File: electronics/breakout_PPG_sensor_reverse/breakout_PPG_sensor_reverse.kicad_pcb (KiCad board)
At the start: 2 copper layers, 19.1 x 11.5 mm, 4 parts, among them J1 Conn_01x04, J2 Conn_01x04, U1 PPG_sensor

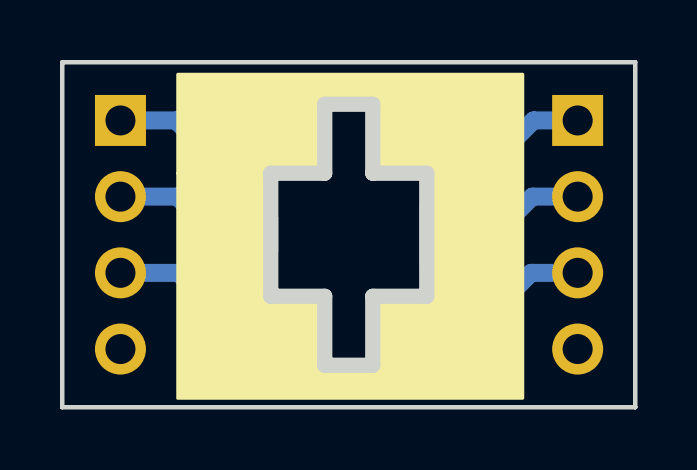
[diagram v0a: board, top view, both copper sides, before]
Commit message: changed cutouts for the PPG sensor, oshpark seems to compute cutouts differently then eagle somehow?
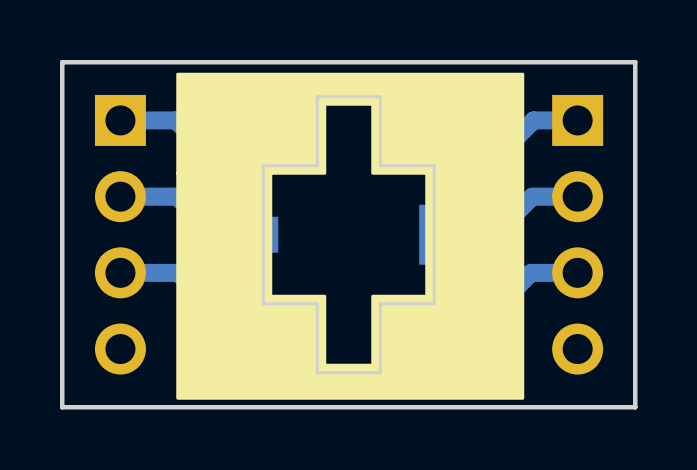
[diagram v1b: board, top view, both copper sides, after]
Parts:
- N2: value 20200709 -> 20200809
- U1: footprint SquantorOpto:PPG_sensor_reverse -> SquantorOpto:PPG_sensor_reverse_PD_parallel
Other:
- outline, holes or cut-outs redrawn
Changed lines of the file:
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@@
-(kicad_pcb (version 20171130) (host pcbnew 5.1.6-c6e7f7d~86~ubuntu19.10.1)
+(kicad_pcb (version 20171130) (host pcbnew 5.1.6-c6e7f7d~87~ubuntu19.10.1)
   (general
     (thickness 1.6)
@@
   )
   (setup
-    (last_trace_width 0.6)
+    (last_trace_width 0.1524)
     (user_trace_width 0.1524)
     (user_trace_width 0.2)
@@
     (uvia_min_size 0.381)
     (uvia_min_drill 0.254)
-    (edge_width 0.508)
+    (edge_width 0.1)
     (segment_width 0.2)
     (pcb_text_width 0.3)
@@
     (add_net /VSS)
   )
-  (module SquantorOpto:PPG_sensor_reverse (layer F.Cu)
+  (module SquantorOpto:PPG_sensor_reverse_PD_parallel (layer F.Cu)
     (at 162.55 101.6)
-    (descr "combination of SFH2440 reverse mount with 1206 reverse mount LEDS")
+    (descr "combination of SFH2440 reverse mount parallel with 3216 reverse mount LEDS")
     (tags "PPG sensor")
-    (fp_text reference U1 (at 0 -5) (layer B.SilkS)
-      (effects (font (size 1 1) (thickness 0.15)) (justify mirror))
-    )
-    (fp_text value PPG_sensor (at 0 4.6) (layer B.Fab)
+    (fp_text reference U1 (at 0 -5.2) (layer B.SilkS)
+      (effects (font (size 1 1) (thickness 0.15)) (justify mirror))
+    )
+    (fp_text value PPG_sensor (at 0 5) (layer B.Fab)
       (effects (font (size 1 1) (thickness 0.15)) (justify mirror))
     )
@@
       (effects (font (size 1 1) (thickness 0.15)) (justify mirror))
     )
+    (fp_line (start 1.8 1.8) (end -1.8 1.8) (layer B.CrtYd) (width 0.05))
+    (fp_line (start 1.8 -9.4) (end 1.8 1.8) (layer B.CrtYd) (width 0.05))
+    (fp_line (start -1.8 -9.4) (end 1.8 -9.4) (layer B.CrtYd) (width 0.05))
+    (fp_line (start -1.8 1.8) (end -1.8 -9.4) (layer B.CrtYd) (width 0.05))
+    (fp_line (start -1.33 1.33) (end 0 1.33) (layer B.SilkS) (width 0.12))
+    (fp_line (start -1.33 0) (end -1.33 1.33) (layer B.SilkS) (width 0.12))
+    (fp_line (start -1.33 -1.27) (end 1.33 -1.27) (layer B.SilkS) (width 0.12))
+    (fp_line (start 1.33 -1.27) (end 1.33 -8.95) (layer B.SilkS) (width 0.12))
+    (fp_line (start -1.33 -1.27) (end -1.33 -8.95) (layer B.SilkS) (width 0.12))
+    (fp_line (start -1.33 -8.95) (end 1.33 -8.95) (layer B.SilkS) (width 0.12))
+    (fp_line (start -1.27 0.635) (end -0.635 1.27) (layer B.Fab) (width 0.1))
+    (fp_line (start -1.27 -8.89) (end -1.27 0.635) (layer B.Fab) (width 0.1))
+    (fp_line (start 1.27 -8.89) (end -1.27 -8.89) (layer B.Fab) (width 0.1))
+    (fp_line (start 1.27 1.27) (end 1.27 -8.89) (layer B.Fab) (width 0.1))
     (fp_line (start -0.635 1.27) (end 1.27 1.27) (layer B.Fab) (width 0.1))
-    (fp_line (start 1.27 1.27) (end 1.27 -8.89) (layer B.Fab) (width 0.1))
-    (fp_line (start 1.27 -8.89) (end -1.27 -8.89) (layer B.Fab) (width 0.1))
-    (fp_line (start -1.27 -8.89) (end -1.27 0.635) (layer B.Fab) (width 0.1))
-    (fp_line (start -1.27 0.635) (end -0.635 1.27) (layer B.Fab) (width 0.1))
-    (fp_line (start -1.33 -8.95) (end 1.33 -8.95) (layer B.SilkS) (width 0.12))
-    (fp_line (start -1.33 -1.27) (end -1.33 -8.95) (layer B.SilkS) (width 0.12))
-    (fp_line (start 1.33 -1.27) (end 1.33 -8.95) (layer B.SilkS) (width 0.12))
-    (fp_line (start -1.33 -1.27) (end 1.33 -1.27) (layer B.SilkS) (width 0.12))
-    (fp_line (start -1.33 0) (end -1.33 1.33) (layer B.SilkS) (width 0.12))
-    (fp_line (start -1.33 1.33) (end 0 1.33) (layer B.SilkS) (width 0.12))
-    (fp_line (start -1.8 1.8) (end -1.8 -9.4) (layer B.CrtYd) (width 0.05))
-    (fp_line (start -1.8 -9.4) (end 1.8 -9.4) (layer B.CrtYd) (width 0.05))
-    (fp_line (start 1.8 -9.4) (end 1.8 1.8) (layer B.CrtYd) (width 0.05))
-    (fp_line (start 1.8 1.8) (end -1.8 1.8) (layer B.CrtYd) (width 0.05))
     (fp_text user %R (at 0 -3.81 270) (layer B.Fab)
       (effects (font (size 1 1) (thickness 0.15)) (justify mirror))
@@
       (effects (font (size 1 1) (thickness 0.15)) (justify mirror))
     )
+    (fp_line (start 1.8 1.8) (end -1.8 1.8) (layer B.CrtYd) (width 0.05))
+    (fp_line (start 1.8 -9.4) (end 1.8 1.8) (layer B.CrtYd) (width 0.05))
+    (fp_line (start -1.8 -9.4) (end 1.8 -9.4) (layer B.CrtYd) (width 0.05))
+    (fp_line (start -1.8 1.8) (end -1.8 -9.4) (layer B.CrtYd) (width 0.05))
+    (fp_line (start -1.33 1.33) (end 0 1.33) (layer B.SilkS) (width 0.12))
+    (fp_line (start -1.33 0) (end -1.33 1.33) (layer B.SilkS) (width 0.12))
+    (fp_line (start -1.33 -1.27) (end 1.33 -1.27) (layer B.SilkS) (width 0.12))
+    (fp_line (start 1.33 -1.27) (end 1.33 -8.95) (layer B.SilkS) (width 0.12))
+    (fp_line (start -1.33 -1.27) (end -1.33 -8.95) (layer B.SilkS) (width 0.12))
+    (fp_line (start -1.33 -8.95) (end 1.33 -8.95) (layer B.SilkS) (width 0.12))
+    (fp_line (start -1.27 0.635) (end -0.635 1.27) (layer B.Fab) (width 0.1))
+    (fp_line (start -1.27 -8.89) (end -1.27 0.635) (layer B.Fab) (width 0.1))
+    (fp_line (start 1.27 -8.89) (end -1.27 -8.89) (layer B.Fab) (width 0.1))
+    (fp_line (start 1.27 1.27) (end 1.27 -8.89) (layer B.Fab) (width 0.1))
     (fp_line (start -0.635 1.27) (end 1.27 1.27) (layer B.Fab) (width 0.1))
-    (fp_line (start 1.27 1.27) (end 1.27 -8.89) (layer B.Fab) (width 0.1))
-    (fp_line (start 1.27 -8.89) (end -1.27 -8.89) (layer B.Fab) (width 0.1))
-    (fp_line (start -1.27 -8.89) (end -1.27 0.635) (layer B.Fab) (width 0.1))
-    (fp_line (start -1.27 0.635) (end -0.635 1.27) (layer B.Fab) (width 0.1))
-    (fp_line (start -1.33 -8.95) (end 1.33 -8.95) (layer B.SilkS) (width 0.12))
-    (fp_line (start -1.33 -1.27) (end -1.33 -8.95) (layer B.SilkS) (width 0.12))
-    (fp_line (start 1.33 -1.27) (end 1.33 -8.95) (layer B.SilkS) (width 0.12))
-    (fp_line (start -1.33 -1.27) (end 1.33 -1.27) (layer B.SilkS) (width 0.12))
-    (fp_line (start -1.33 0) (end -1.33 1.33) (layer B.SilkS) (width 0.12))
-    (fp_line (start -1.33 1.33) (end 0 1.33) (layer B.SilkS) (width 0.12))
-    (fp_line (start -1.8 1.8) (end -1.8 -9.4) (layer B.CrtYd) (width 0.05))
-    (fp_line (start -1.8 -9.4) (end 1.8 -9.4) (layer B.CrtYd) (width 0.05))
-    (fp_line (start 1.8 -9.4) (end 1.8 1.8) (layer B.CrtYd) (width 0.05))
-    (fp_line (start 1.8 1.8) (end -1.8 1.8) (layer B.CrtYd) (width 0.05))
     (fp_text user %R (at 0 -3.81 270) (layer B.Fab)
       (effects (font (size 1 1) (thickness 0.15)) (justify mirror))
@@
       (effects (font (size 1 1) (thickness 0.15)) (justify mirror))
     )
-    (fp_text value 20200709 (at -0.4 0.1 90) (layer B.SilkS)
+    (fp_text value 20200809 (at -0.4 0.1 90) (layer B.SilkS)
       (effects (font (size 1 1) (thickness 0.15)) (justify mirror))
     )
@@
     )
   )
-  (gr_line (start 159.95 103.65) (end 159.95 99.55) (layer Edge.Cuts) (width 0.508))
-  (gr_line (start 161.75 103.65) (end 159.95 103.65) (layer Edge.Cuts) (width 0.508))
-  (gr_line (start 161.75 105.95) (end 161.75 103.65) (layer Edge.Cuts) (width 0.508))
-  (gr_line (start 163.35 105.95) (end 161.75 105.95) (layer Edge.Cuts) (width 0.508))
-  (gr_line (start 163.35 103.65) (end 163.35 105.95) (layer Edge.Cuts) (width 0.508))
-  (gr_line (start 165.15 103.65) (end 163.35 103.65) (layer Edge.Cuts) (width 0.508))
-  (gr_line (start 165.15 99.55) (end 165.15 103.65) (layer Edge.Cuts) (width 0.508))
-  (gr_line (start 163.35 99.55) (end 165.15 99.55) (layer Edge.Cuts) (width 0.508))
-  (gr_line (start 163.35 97.25) (end 163.35 99.55) (layer Edge.Cuts) (width 0.508))
-  (gr_line (start 161.75 97.25) (end 163.35 97.25) (layer Edge.Cuts) (width 0.508))
-  (gr_line (start 161.75 99.55) (end 161.75 97.25) (layer Edge.Cuts) (width 0.508))
-  (gr_line (start 159.95 99.55) (end 161.75 99.55) (layer Edge.Cuts) (width 0.508))
+  (gr_line (start 161.5 103.9) (end 161.5 106.2) (layer Edge.Cuts) (width 0.1))
+  (gr_line (start 159.7 103.9) (end 161.5 103.9) (layer Edge.Cuts) (width 0.1))
+  (gr_line (start 159.7 99.3) (end 159.7 103.9) (layer Edge.Cuts) (width 0.1))
+  (gr_line (start 161.5 99.3) (end 159.7 99.3) (layer Edge.Cuts) (width 0.1))
+  (gr_line (start 161.5 97) (end 161.5 99.3) (layer Edge.Cuts) (width 0.1))
+  (gr_line (start 163.6 97) (end 161.5 97) (layer Edge.Cuts) (width 0.1))
+  (gr_line (start 163.6 99.3) (end 163.6 97) (layer Edge.Cuts) (width 0.1))
+  (gr_line (start 165.4 99.3) (end 163.6 99.3) (layer Edge.Cuts) (width 0.1))
+  (gr_line (start 165.4 103.9) (end 165.4 99.3) (layer Edge.Cuts) (width 0.1))
+  (gr_line (start 163.6 103.9) (end 165.4 103.9) (layer Edge.Cuts) (width 0.1))
+  (gr_line (start 163.6 106.2) (end 163.6 103.9) (layer Edge.Cuts) (width 0.1))
+  (gr_line (start 161.5 106.2) (end 163.6 106.2) (layer Edge.Cuts) (width 0.1))
   (gr_line (start 153 107.35) (end 153 95.85) (layer Edge.Cuts) (width 0.15))
   (gr_line (start 172.1 107.35) (end 153 107.35) (layer Edge.Cuts) (width 0.15))
